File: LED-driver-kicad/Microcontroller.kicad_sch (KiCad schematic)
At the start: 0 parts

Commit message: chore: update Microcontroller.kicad_sch
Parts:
- added U6: PIC16F18026-ISL, Package_SO:SOIC-14_3.9x8.7mm_P1.27mm, symbol MCU_Microchip_PIC1616f1829-ISL:PIC16F18026-ISL
- added U9: 25AA02E64-I/SN, SOIC8_4P9X3P9MC_MCH, symbol 25AA02E64-I/SN:25AA02E64-I_SN
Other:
- note added: "EEPROM w/ pre-programmed MAC address"
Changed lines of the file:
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@@
 (kicad_sch (version 20230121) (generator eeschema)
   (paper "A4")
+  (text "EEPROM w/ pre-programmed MAC address" (at 60.96 137.16 0)
+    (effects (font (size 1.27 1.27)) (justify left bottom))
+  )
+  (symbol (lib_id "25AA02E64-I/SN:25AA02E64-I_SN") (at 53.34 120.65 0) (unit 1)
+    (in_bom yes) (on_board yes) (dnp no) (fields_autoplaced)
+    (property "Reference" "U9" (at 73.66 110.49 0)
+      (effects (font (size 1.524 1.524)))
+    )
+    (property "Value" "25AA02E64-I/SN" (at 73.66 113.03 0)
+      (effects (font (size 1.524 1.524)))
+    )
+    (property "Footprint" "SOIC8_4P9X3P9MC_MCH" (at 53.34 120.65 0)
+      (effects (font (size 1.27 1.27) italic) hide)
+    )
+    (property "Datasheet" "25AA02E64-I/SN" (at 53.34 120.65 0)
+      (effects (font (size 1.27 1.27) italic) hide)
+    )
+    (pin "1")
+    (pin "2")
+    (pin "3")
+    (pin "4")
+    (pin "5")
+    (pin "6")
+    (pin "7")
+    (pin "8")
+    (instances
+      (project "LED-driver-kicad"
+        (path "/2b071084-2ab6-4896-84cc-45b211479417/359e4c60-3d39-46c5-bd25-b25d83369b39"
+          (reference "U9") (unit 1)
+        )
+        (path "/2b071084-2ab6-4896-84cc-45b211479417/9127cd83-cae7-424d-ad3b-8a9e0439da28"
+          (reference "U9") (unit 1)
+        )
+      )
+    )
+  )
+  (symbol (lib_id "MCU_Microchip_PIC1616f1829-ISL:PIC16F18026-ISL") (at 140.97 85.09 0) (unit 1)
+    (in_bom yes) (on_board yes) (dnp no) (fields_autoplaced)
+    (property "Reference" "U6" (at 143.1641 60.96 0)
+      (effects (font (size 1.27 1.27)) (justify left))
+    )
+    (property "Value" "PIC16F18026-ISL" (at 143.1641 63.5 0)
+      (effects (font (size 1.27 1.27)) (justify left))
+    )
+    (property "Footprint" "Package_SO:SOIC-14_3.9x8.7mm_P1.27mm" (at 140.97 99.06 0)
+      (effects (font (size 1.27 1.27)) hide)
+    )
+    (property "Datasheet" "https://ww1.microchip.com/downloads/aemDocuments/documents/MCU08/ProductDocuments/DataSheets/PIC16F18026-46-Microcontroller-Data-Sheet-40002415.pdf" (at 142.24 96.52 0)
+      (effects (font (size 1.27 1.27)) hide)
+    )
+    (pin "1")
+    (pin "10")
+    (pin "11")
+    (pin "12")
+    (pin "13")
+    (pin "14")
+    (pin "2")
+    (pin "3")
+    (pin "4")
+    (pin "5")
+    (pin "6")
+    (pin "7")
+    (pin "8")
+    (pin "9")
+    (instances
+      (project "LED-driver-kicad"
+        (path "/2b071084-2ab6-4896-84cc-45b211479417/9127cd83-cae7-424d-ad3b-8a9e0439da28"
+          (reference "U6") (unit 1)
+        )
+      )
+    )
+  )
 )

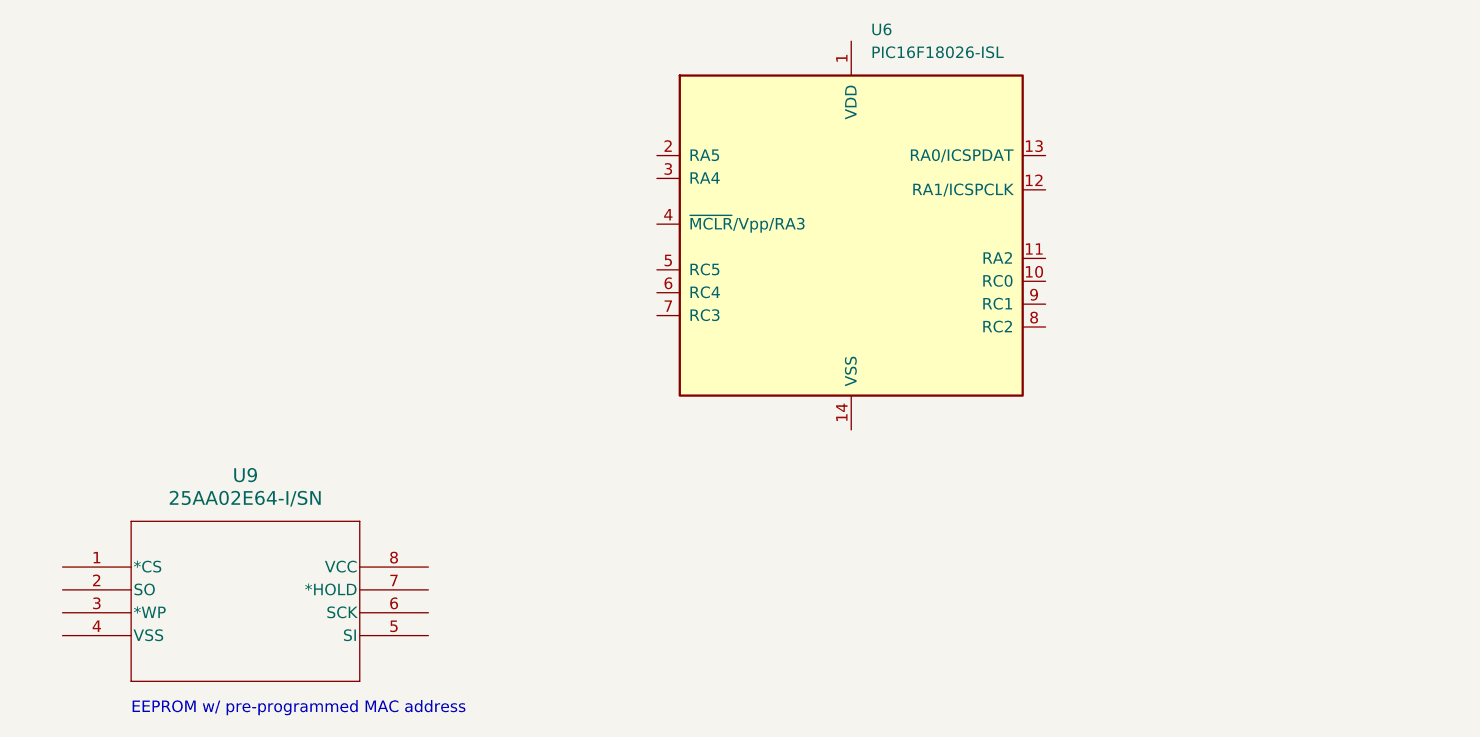
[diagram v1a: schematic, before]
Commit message: update main schematic sheet and microcontroller
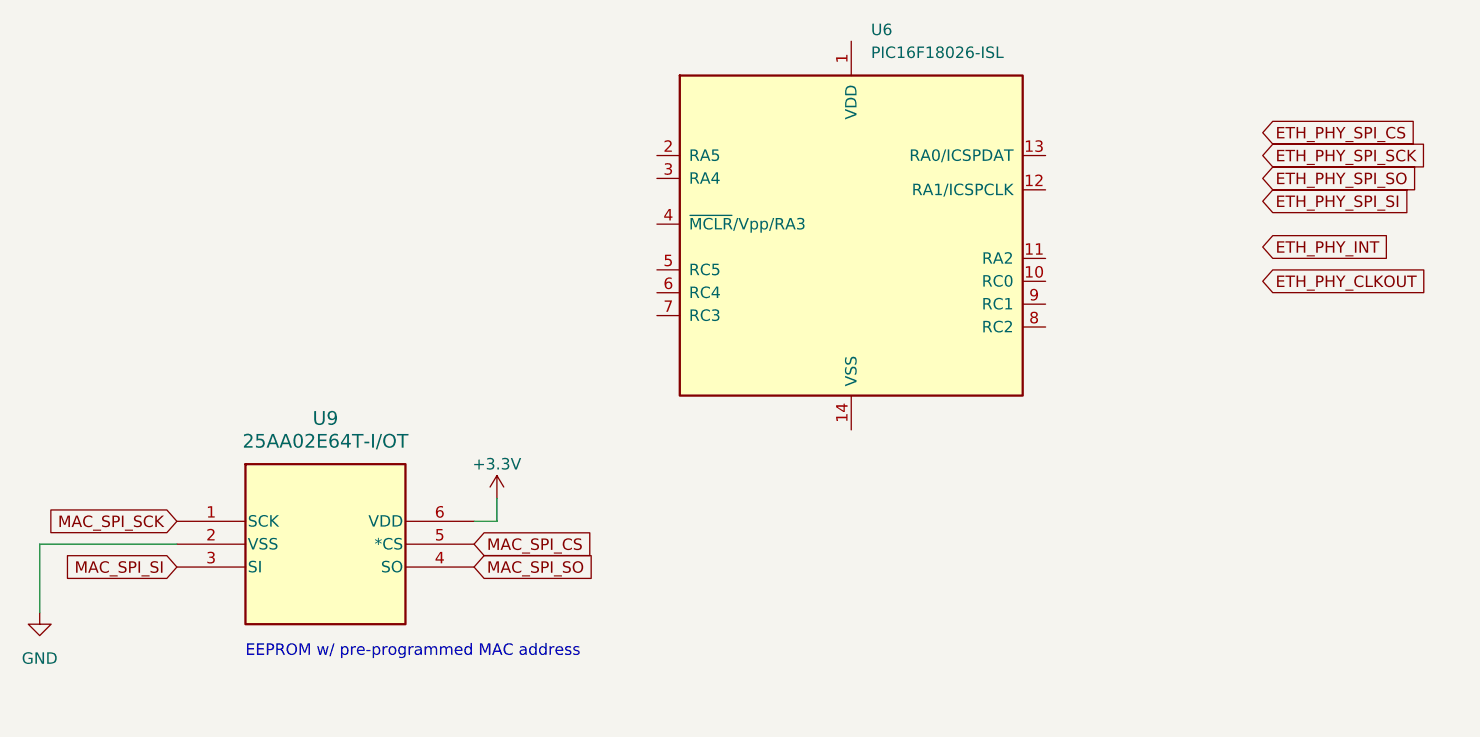
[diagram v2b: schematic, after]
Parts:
- removed U9: 25AA02E64-I/SN, SOIC8_4P9X3P9MC_MCH, symbol 25AA02E64-I/SN:25AA02E64-I_SN
- added U9: 25AA02E64T-I/OT, SOT-23-6_MC_MCH, symbol Memory_Microchip_25AA02E64T-IOT:25AA02E64T-I_OT
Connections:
- new net +3.3V: U9.6 (VDD)
- new net GND: U9.2 (VSS)
- new net MAC_SPI_CS: U9.5 (*CS)
- new net MAC_SPI_SCK: U9.1 (SCK)
- new net MAC_SPI_SI: U9.3 (SI)
- new net MAC_SPI_SO: U9.4 (SO)
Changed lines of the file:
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@@
 (kicad_sch (version 20230121) (generator eeschema)
   (paper "A4")
-  (text "EEPROM w/ pre-programmed MAC address" (at 60.96 137.16 0)
+  (wire (pts (xy 101.6 115.57) (xy 101.6 113.03))
+    (stroke (width 0) (type default))
+  )
+  (wire (pts (xy 50.8 118.11) (xy 66.04 118.11))
+    (stroke (width 0) (type default))
+  )
+  (wire (pts (xy 50.8 125.73) (xy 50.8 118.11))
+    (stroke (width 0) (type default))
+  )
+  (wire (pts (xy 99.06 115.57) (xy 101.6 115.57))
+    (stroke (width 0) (type default))
+  )
+  (text "EEPROM w/ pre-programmed MAC address" (at 73.66 130.81 0)
     (effects (font (size 1.27 1.27)) (justify left bottom))
   )
-  (symbol (lib_id "25AA02E64-I/SN:25AA02E64-I_SN") (at 53.34 120.65 0) (unit 1)
+  (global_label "MAC_SPI_SO" (shape input) (at 99.06 120.65 0) (fields_autoplaced)
+    (effects (font (size 1.27 1.27)) (justify left))
+    (property "Intersheetrefs" "${INTERSHEET_REFS}" (at 113.4147 120.65 0)
+      (effects (font (size 1.27 1.27)) (justify left) hide)
+    )
+  )
+  (global_label "ETH_PHY_CLKOUT" (shape input) (at 186.69 88.9 0) (fields_autoplaced)
+    (effects (font (size 1.27 1.27)) (justify left))
+    (property "Intersheetrefs" "${INTERSHEET_REFS}" (at 205.9433 88.9 0)
+      (effects (font (size 1.27 1.27)) (justify left) hide)
+    )
+  )
+  (global_label "MAC_SPI_SI" (shape input) (at 66.04 120.65 180) (fields_autoplaced)
+    (effects (font (size 1.27 1.27)) (justify right))
+    (property "Intersheetrefs" "${INTERSHEET_REFS}" (at 52.411 120.65 0)
+      (effects (font (size 1.27 1.27)) (justify right) hide)
+    )
+  )
+  (global_label "ETH_PHY_INT" (shape input) (at 186.69 85.09 0) (fields_autoplaced)
+    (effects (font (size 1.27 1.27)) (justify left))
+    (property "Intersheetrefs" "${INTERSHEET_REFS}" (at 201.6495 85.09 0)
+      (effects (font (size 1.27 1.27)) (justify left) hide)
+    )
+  )
+  (global_label "ETH_PHY_SPI_SI" (shape input) (at 186.69 80.01 0) (fields_autoplaced)
+    (effects (font (size 1.27 1.27)) (justify left))
+    (property "Intersheetrefs" "${INTERSHEET_REFS}" (at 204.6128 80.01 0)
+      (effects (font (size 1.27 1.27)) (justify left) hide)
+    )
+  )
+  (global_label "ETH_PHY_SPI_SO" (shape input) (at 186.69 77.47 0) (fields_autoplaced)
+    (effects (font (size 1.27 1.27)) (justify left))
+    (property "Intersheetrefs" "${INTERSHEET_REFS}" (at 205.3385 77.47 0)
+      (effects (font (size 1.27 1.27)) (justify left) hide)
+    )
+  )
+  (global_label "ETH_PHY_SPI_SCK" (shape input) (at 186.69 74.93 0) (fields_autoplaced)
+    (effects (font (size 1.27 1.27)) (justify left))
+    (property "Intersheetrefs" "${INTERSHEET_REFS}" (at 206.548 74.93 0)
+      (effects (font (size 1.27 1.27)) (justify left) hide)
+    )
+  )
+  (global_label "ETH_PHY_SPI_CS" (shape input) (at 186.69 72.39 0) (fields_autoplaced)
+    (effects (font (size 1.27 1.27)) (justify left))
+    (property "Intersheetrefs" "${INTERSHEET_REFS}" (at 205.278 72.39 0)
+      (effects (font (size 1.27 1.27)) (justify left) hide)
+    )
+  )
+  (global_label "MAC_SPI_SCK" (shape input) (at 66.04 115.57 180) (fields_autoplaced)
+    (effects (font (size 1.27 1.27)) (justify right))
+    (property "Intersheetrefs" "${INTERSHEET_REFS}" (at 50.4758 115.57 0)
+      (effects (font (size 1.27 1.27)) (justify right) hide)
+    )
+  )
+  (global_label "MAC_SPI_CS" (shape input) (at 99.06 118.11 0) (fields_autoplaced)
+    (effects (font (size 1.27 1.27)) (justify left))
+    (property "Intersheetrefs" "${INTERSHEET_REFS}" (at 113.3542 118.11 0)
+      (effects (font (size 1.27 1.27)) (justify left) hide)
+    )
+  )
+  (symbol (lib_id "power:GND") (at 50.8 125.73 0) (unit 1)
     (in_bom yes) (on_board yes) (dnp no) (fields_autoplaced)
-    (property "Reference" "U9" (at 73.66 110.49 0)
+    (property "Reference" "#PWR04" (at 50.8 132.08 0)
+      (effects (font (size 1.27 1.27)) hide)
+    )
+    (property "Value" "GND" (at 50.8 130.81 0)
+      (effects (font (size 1.27 1.27)))
+    )
+    (property "Footprint" "" (at 50.8 125.73 0)
+      (effects (font (size 1.27 1.27)) hide)
+    )
+    (property "Datasheet" "" (at 50.8 125.73 0)
+      (effects (font (size 1.27 1.27)) hide)
+    )
+    (pin "1")
+    (instances
+      (project "LED-driver-kicad"
+        (path "/2b071084-2ab6-4896-84cc-45b211479417"
+          (reference "#PWR04") (unit 1)
+        )
+        (path "/2b071084-2ab6-4896-84cc-45b211479417/9127cd83-cae7-424d-ad3b-8a9e0439da28"
+          (reference "#PWR04") (unit 1)
+        )
+      )
+    )
+  )
+  (symbol (lib_id "power:+3.3V") (at 101.6 113.03 0) (unit 1)
+    (in_bom yes) (on_board yes) (dnp no)
+    (property "Reference" "#PWR05" (at 101.6 116.84 0)
+      (effects (font (size 1.27 1.27)) hide)
+    )
+    (property "Value" "+3.3V" (at 101.6 109.22 0)
+      (effects (font (size 1.27 1.27)))
+    )
+    (property "Footprint" "" (at 101.6 113.03 0)
+      (effects (font (size 1.27 1.27)) hide)
+    )
+    (property "Datasheet" "" (at 101.6 113.03 0)
+      (effects (font (size 1.27 1.27)) hide)
+    )
+    (pin "1")
+    (instances
+      (project "LED-driver-kicad"
+        (path "/2b071084-2ab6-4896-84cc-45b211479417"
+          (reference "#PWR05") (unit 1)
+        )
+        (path "/2b071084-2ab6-4896-84cc-45b211479417/9127cd83-cae7-424d-ad3b-8a9e0439da28"
+          (reference "#PWR05") (unit 1)
+        )
+      )
+    )
+  )
+  (symbol (lib_id "Memory_Microchip_25AA02E64T-IOT:25AA02E64T-I_OT") (at 82.55 118.11 0) (unit 1)
+    (in_bom yes) (on_board yes) (dnp no) (fields_autoplaced)
+    (property "Reference" "U9" (at 82.55 104.14 0)
       (effects (font (size 1.524 1.524)))
     )
-    (property "Value" "25AA02E64-I/SN" (at 73.66 113.03 0)
+    (property "Value" "25AA02E64T-I/OT" (at 82.55 106.68 0)
       (effects (font (size 1.524 1.524)))
     )
-    (property "Footprint" "SOIC8_4P9X3P9MC_MCH" (at 53.34 120.65 0)
+    (property "Footprint" "SOT-23-6_MC_MCH" (at 82.55 130.81 0)
       (effects (font (size 1.27 1.27) italic) hide)
     )
-    (property "Datasheet" "25AA02E64-I/SN" (at 53.34 120.65 0)
+    (property "Datasheet" "25AA02E64T-I/OT" (at 82.55 128.27 0)
       (effects (font (size 1.27 1.27) italic) hide)
     )
@@
     (pin "5")
     (pin "6")
-    (pin "7")
-    (pin "8")
     (instances
       (project "LED-driver-kicad"
-        (path "/2b071084-2ab6-4896-84cc-45b211479417/359e4c60-3d39-46c5-bd25-b25d83369b39"
-          (reference "U9") (unit 1)
-        )
         (path "/2b071084-2ab6-4896-84cc-45b211479417/9127cd83-cae7-424d-ad3b-8a9e0439da28"
           (reference "U9") (unit 1)
